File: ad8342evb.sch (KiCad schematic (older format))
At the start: 95 parts, among them J1 PWR_in_direct, J10 Bat, J11 3V3, J12 PWR_Jumper, J13 TP1, J14 TP1, J15 TP_PWR, J16 TP2, J17 TP3, J2 RF_in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

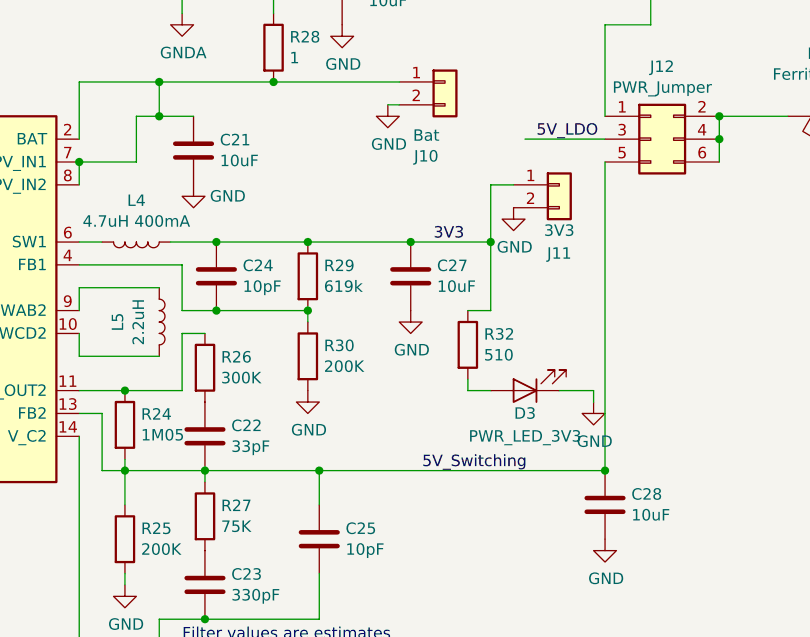
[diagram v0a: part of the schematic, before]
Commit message: fixed mistake in schematic
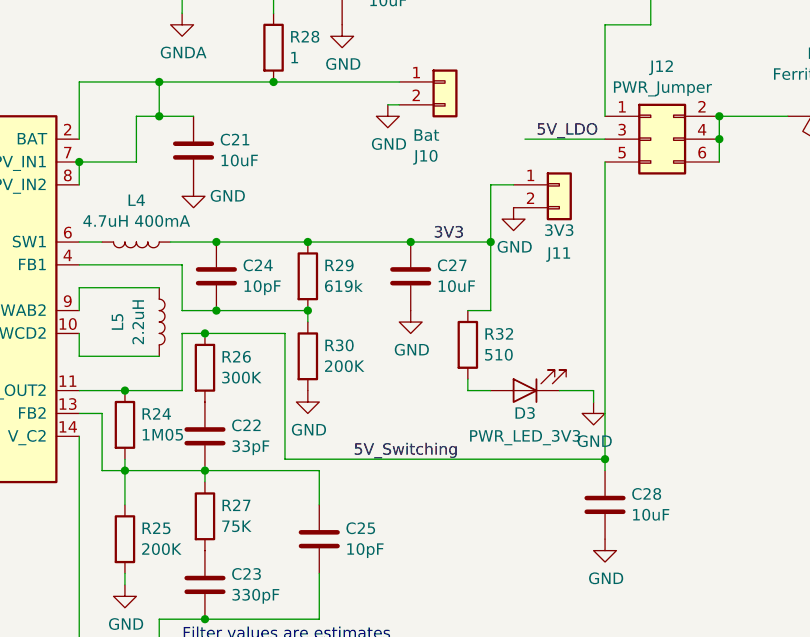
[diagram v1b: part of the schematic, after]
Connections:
- net 5V_Switching: now also R24.1, R26.1, U3.11 (V_OUT2); no longer C22.2, C25.1, R24.2, R25.1, R27.1, U3.13 (FB2)
- new net: C22.2, C25.1, R24.2, R25.1, R27.1, U3.13 (FB2)
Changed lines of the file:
@@
 	4200 7000 4700 7000
 Wire Wire Line
-	5950 5650 5950 7000
-Connection ~ 5950 7000
+	5950 5650 5950 6950
 $Comp
 L Device:C C25
@@
 Wire Wire Line
 	4700 7000 4700 7150
-Connection ~ 4700 7000
-Wire Wire Line
-	4700 7000 5950 7000
 Wire Wire Line
 	4700 7450 4700 7650
@@
 Text Label 5200 6000 0    50   ~ 0
 3V3
-Text Label 5150 7000 0    50   ~ 0
+Text Label 4850 6950 0    50   ~ 0
 5V_Switching
 Connection ~ 5100 6000
@@
 	3650 7750 3650 6850
 Connection ~ 4200 7650
+Wire Wire Line
+	4200 6400 4550 6400
+Wire Wire Line
+	4550 6400 4550 6950
+Wire Wire Line
+	4550 6950 5950 6950
+Connection ~ 4200 6400
+Connection ~ 5950 6950
+Wire Wire Line
+	5950 6950 5950 7000
 $EndSCHEMATC

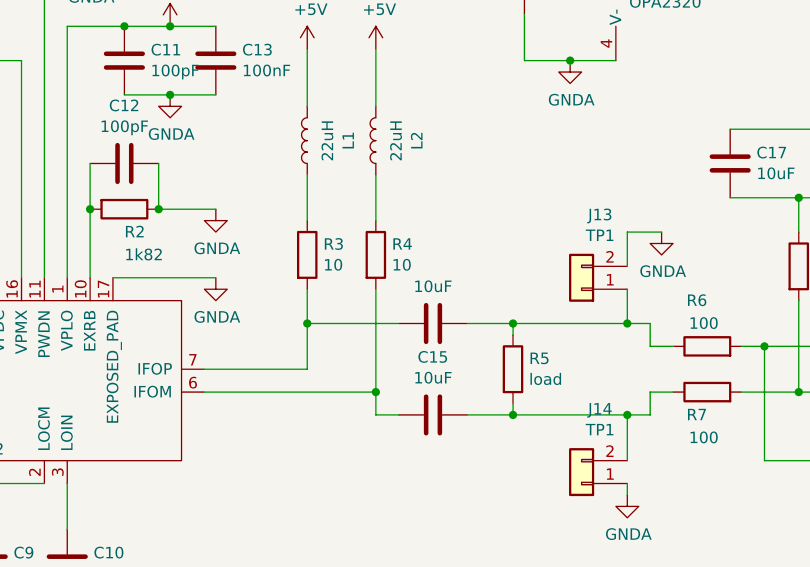
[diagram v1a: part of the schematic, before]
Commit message: added DC bias resistor for OPAMP
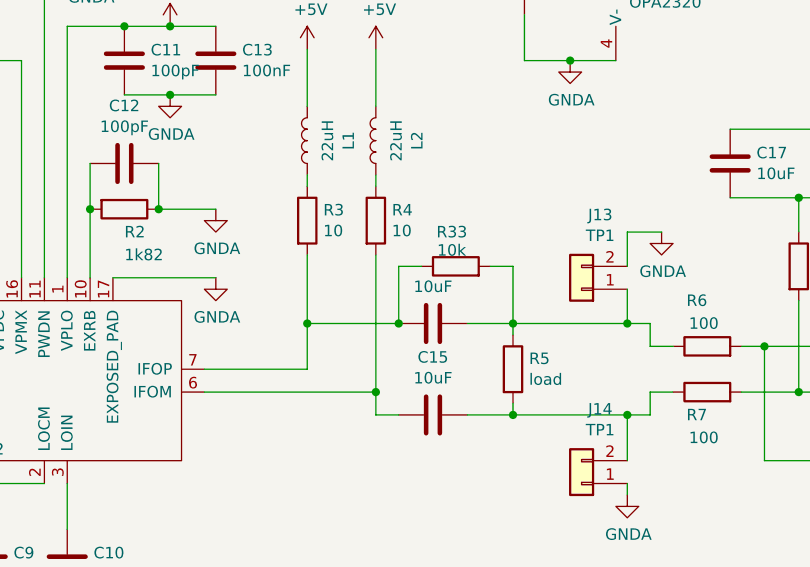
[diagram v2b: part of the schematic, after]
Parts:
- added R33: 10k, Resistor_SMD:R_0805_2012Metric_Pad1.15x1.40mm_HandSolder, symbol Device:R
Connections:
- net at C14.1, R3.2, U4.7 (IFOP): now also R33.1
- net at C14.2, J13.1 (Pin_1), R5.1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: now also R33.2
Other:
- moved on the sheet: R3, R4
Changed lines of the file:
@@
 L Device:R R3
 U 1 1 5F19B732
-P 5450 2500
-F 0 "R3" H 5520 2546 50  0000 L CNN
-F 1 "10" H 5520 2455 50  0000 L CNN
-F 2 "Resistor_SMD:R_0805_2012Metric_Pad1.15x1.40mm_HandSolder" V 5380 2500 50  0001 C CNN
-F 3 "~" H 5450 2500 50  0001 C CNN
-	1    5450 2500
+P 5450 2350
+F 0 "R3" H 5520 2396 50  0000 L CNN
+F 1 "10" H 5520 2305 50  0000 L CNN
+F 2 "Resistor_SMD:R_0805_2012Metric_Pad1.15x1.40mm_HandSolder" V 5380 2350 50  0001 C CNN
+F 3 "~" H 5450 2350 50  0001 C CNN
+	1    5450 2350
 	1    0    0    -1
 $EndComp
@@
 L Device:R R4
 U 1 1 5F19BCA9
-P 5750 2500
-F 0 "R4" H 5820 2546 50  0000 L CNN
-F 1 "10" H 5820 2455 50  0000 L CNN
-F 2 "Resistor_SMD:R_0805_2012Metric_Pad1.15x1.40mm_HandSolder" V 5680 2500 50  0001 C CNN
-F 3 "~" H 5750 2500 50  0001 C CNN
-	1    5750 2500
-	1    0    0    -1
-$EndComp
-Wire Wire Line
-	5450 2650 5450 2800
+P 5750 2350
+F 0 "R4" H 5820 2396 50  0000 L CNN
+F 1 "10" H 5820 2305 50  0000 L CNN
+F 2 "Resistor_SMD:R_0805_2012Metric_Pad1.15x1.40mm_HandSolder" V 5680 2350 50  0001 C CNN
+F 3 "~" H 5750 2350 50  0001 C CNN
+	1    5750 2350
+	1    0    0    -1
+$EndComp
 Wire Wire Line
 	5450 2800 5850 2800
-Wire Wire Line
-	5750 2650 5750 3100
 $Comp
 L power:+5V #PWR0104
@@
 	1    0    0    -1
 $EndComp
-Wire Wire Line
-	5750 2150 5750 2350
 Wire Wire Line
 	4100 2600 4100 1950
@@
 Wire Wire Line
 	750  6200 750  6650
-Wire Wire Line
-	5450 2350 5450 2150
 $Comp
 L Connector_Generic:Conn_02x03_Odd_Even J4
@@
 Wire Wire Line
 	5950 6950 5950 7000
+Wire Wire Line
+	5750 2150 5750 2200
+Wire Wire Line
+	5450 2150 5450 2200
+Wire Wire Line
+	5450 2500 5450 2800
+Wire Wire Line
+	5750 2500 5750 3100
+$Comp
+L Device:R R33
+U 1 1 5F36EBE7
+P 6100 2550
+F 0 "R33" V 6250 2500 50  0000 L CNN
+F 1 "10k" V 6170 2505 50  0000 L CNN
+F 2 "Resistor_SMD:R_0805_2012Metric_Pad1.15x1.40mm_HandSolder" V 6030 2550 50  0001 C CNN
+F 3 "~" H 6100 2550 50  0001 C CNN
+	1    6100 2550
+	0    -1   -1   0
+$EndComp
+Wire Wire Line
+	5950 2550 5850 2550
+Wire Wire Line
+	5850 2550 5850 2800
+Connection ~ 5850 2800
+Wire Wire Line
+	6250 2550 6350 2550
+Wire Wire Line
+	6350 2550 6350 2800
 $EndSCHEMATC

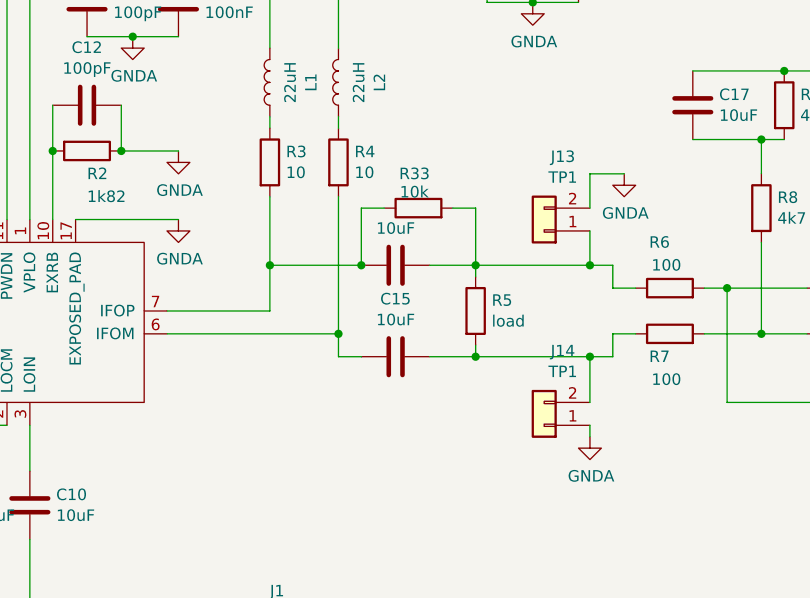
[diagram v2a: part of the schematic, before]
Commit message: moved bias resistor to correct location
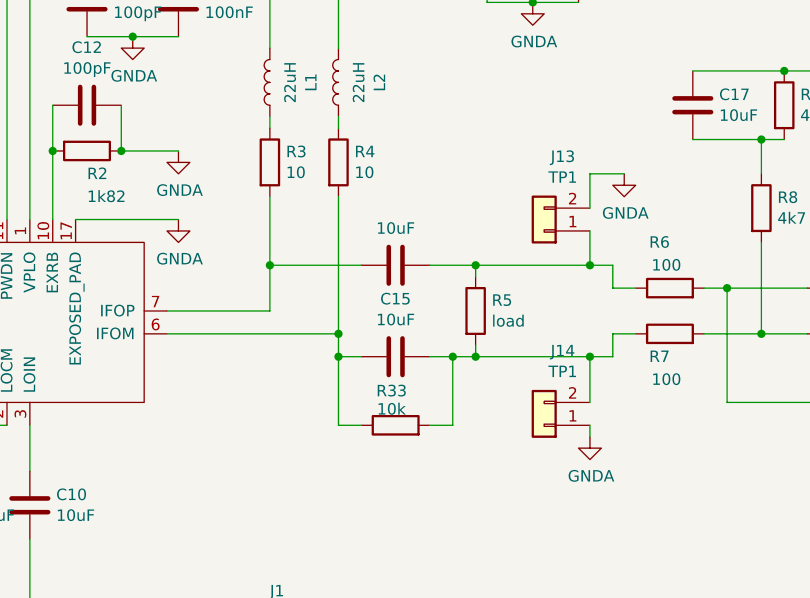
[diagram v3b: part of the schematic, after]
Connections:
- net at C15.1, R4.2, U4.6 (IFOM): now also R33.1
- net at C14.1, R3.2, U4.7 (IFOP): no longer R33.1
- net at C14.2, J13.1 (Pin_1), R5.1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: no longer R33.2
- net at C15.2, J14.2 (Pin_2), R5.2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: now also R33.2
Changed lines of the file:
@@
 	6350 3150 6350 3200
 Wire Wire Line
-	6350 3200 6150 3200
+	6350 3200 6250 3200
 $Comp
 L user_Operational_Amplifier:OPA2320 U2
@@
 $Comp
 L Device:R R33
-U 1 1 5F36EBE7
-P 6100 2550
-F 0 "R33" V 6250 2500 50  0000 L CNN
-F 1 "10k" V 6170 2505 50  0000 L CNN
-F 2 "Resistor_SMD:R_0805_2012Metric_Pad1.15x1.40mm_HandSolder" V 6030 2550 50  0001 C CNN
-F 3 "~" H 6100 2550 50  0001 C CNN
-	1    6100 2550
+U 1 1 5F30BE35
+P 6000 3500
+F 0 "R33" V 6150 3450 50  0000 L CNN
+F 1 "10k" V 6070 3455 50  0000 L CNN
+F 2 "Resistor_SMD:R_0805_2012Metric_Pad1.15x1.40mm_HandSolder" V 5930 3500 50  0001 C CNN
+F 3 "~" H 6000 3500 50  0001 C CNN
+	1    6000 3500
 	0    -1   -1   0
 $EndComp
 Wire Wire Line
-	5950 2550 5850 2550
-Wire Wire Line
-	5850 2550 5850 2800
-Connection ~ 5850 2800
-Wire Wire Line
-	6250 2550 6350 2550
-Wire Wire Line
-	6350 2550 6350 2800
+	5850 3500 5750 3500
+Wire Wire Line
+	6150 3500 6250 3500
+Wire Wire Line
+	5750 3500 5750 3200
+Connection ~ 5750 3200
+Wire Wire Line
+	6250 3500 6250 3200
+Connection ~ 6250 3200
+Wire Wire Line
+	6250 3200 6150 3200
 $EndSCHEMATC

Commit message: modified bias circuit
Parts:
- removed R9: 4k7, Resistor_SMD:R_0805_2012Metric_Pad1.15x1.40mm_HandSolder, symbol Device:R
- added R?: 10k, Resistor_SMD:R_0805_2012Metric_Pad1.15x1.40mm_HandSolder, symbol Device:R
- R33: value 10k -> x
- R8: value 4k7 -> 10k
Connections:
- net +5V: now also R?.2
- net GNDA: now also R8.1
- net at R7.2, R8.2, U2.3 (+): now also C17.2, R?.1
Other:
- moved on the sheet: C17, R10, R8
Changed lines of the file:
@@
 L Device:R R10
 U 1 1 5F1FA385
-P 8000 3400
-F 0 "R10" V 7900 3350 50  0000 L CNN
-F 1 "4k7" V 7800 3350 50  0000 L CNN
-F 2 "Resistor_SMD:R_0805_2012Metric_Pad1.15x1.40mm_HandSolder" V 7930 3400 50  0001 C CNN
-F 3 "~" H 8000 3400 50  0001 C CNN
-	1    8000 3400
+P 8000 2550
+F 0 "R10" V 7900 2500 50  0000 L CNN
+F 1 "4k7" V 7800 2500 50  0000 L CNN
+F 2 "Resistor_SMD:R_0805_2012Metric_Pad1.15x1.40mm_HandSolder" V 7930 2550 50  0001 C CNN
+F 3 "~" H 8000 2550 50  0001 C CNN
+	1    8000 2550
 	0    -1   -1   0
 $EndComp
-Wire Wire Line
-	8400 3000 8400 3400
-Wire Wire Line
-	8400 3400 8150 3400
 $Comp
 L Device:R R8
 U 1 1 5F200A58
-P 7600 2550
-F 0 "R8" H 7670 2596 50  0000 L CNN
-F 1 "4k7" H 7670 2505 50  0000 L CNN
-F 2 "Resistor_SMD:R_0805_2012Metric_Pad1.15x1.40mm_HandSolder" V 7530 2550 50  0001 C CNN
-F 3 "~" H 7600 2550 50  0001 C CNN
-	1    7600 2550
-	1    0    0    -1
+P 7550 3700
+F 0 "R8" H 7650 3650 50  0000 L CNN
+F 1 "10k" H 7650 3750 50  0000 L CNN
+F 2 "Resistor_SMD:R_0805_2012Metric_Pad1.15x1.40mm_HandSolder" V 7480 3700 50  0001 C CNN
+F 3 "~" H 7550 3700 50  0001 C CNN
+	1    7550 3700
+	1    0    0    1
 $EndComp
 $Comp
@@
 	9300 4250 9300 4400
 Wire Wire Line
-	8400 3400 8400 3750
-Wire Wire Line
 	8400 3750 8050 3750
 Wire Wire Line
 	8050 3750 8050 4250
-Connection ~ 8400 3400
 Wire Wire Line
 	9300 4250 9300 3750
@@
 L Device:C C17
 U 1 1 5F280D97
-P 7300 2100
-F 0 "C17" H 7415 2146 50  0000 L CNN
-F 1 "10uF" H 7415 2055 50  0000 L CNN
-F 2 "Capacitor_SMD:C_0805_2012Metric_Pad1.15x1.40mm_HandSolder" H 7338 1950 50  0001 C CNN
-F 3 "~" H 7300 2100 50  0001 C CNN
-	1    7300 2100
-	1    0    0    -1
-$EndComp
-$Comp
-L Device:R R9
-U 1 1 5F284774
-P 7700 2100
-F 0 "R9" H 7770 2146 50  0000 L CNN
-F 1 "4k7" H 7770 2055 50  0000 L CNN
-F 2 "Resistor_SMD:R_0805_2012Metric_Pad1.15x1.40mm_HandSolder" V 7630 2100 50  0001 C CNN
-F 3 "~" H 7700 2100 50  0001 C CNN
-	1    7700 2100
-	1    0    0    -1
-$EndComp
-Wire Wire Line
-	7300 2250 7600 2250
-Wire Wire Line
-	7600 2400 7600 2250
-Connection ~ 7600 2250
-Wire Wire Line
-	7600 2250 7700 2250
-Wire Wire Line
-	7300 1950 7700 1950
+P 7150 3700
+F 0 "C17" H 7250 3650 50  0000 L CNN
+F 1 "10uF" H 7250 3750 50  0000 L CNN
+F 2 "Capacitor_SMD:C_0805_2012Metric_Pad1.15x1.40mm_HandSolder" H 7188 3550 50  0001 C CNN
+F 3 "~" H 7150 3700 50  0001 C CNN
+	1    7150 3700
+	1    0    0    1
+$EndComp
 Wire Wire Line
 	9300 4700 9300 4800
-Wire Wire Line
-	8100 1950 8100 2050
-Wire Wire Line
-	8100 1950 7700 1950
-Connection ~ 7700 1950
 $Comp
 L Device:R R16
@@
 Wire Wire Line
 	8250 4250 8350 4250
-Wire Wire Line
-	7350 2900 7450 2900
-Wire Wire Line
-	7350 3100 7600 3100
-Wire Wire Line
-	7600 2700 7600 3100
-Connection ~ 7600 3100
-Wire Wire Line
-	7600 3100 7800 3100
-Wire Wire Line
-	7450 3400 7450 2900
-Wire Wire Line
-	7450 3400 7850 3400
-Connection ~ 7450 2900
-Wire Wire Line
-	7450 2900 7800 2900
 $Comp
 L Device:R R32
@@
 L power:GNDA #PWR0111
 U 1 1 5F336EFE
-P 8100 2050
-F 0 "#PWR0111" H 8100 1800 50  0001 C CNN
-F 1 "GNDA" H 8105 1877 50  0000 C CNN
-F 2 "" H 8100 2050 50  0001 C CNN
-F 3 "" H 8100 2050 50  0001 C CNN
-	1    8100 2050
-	1    0    0    -1
+P 7350 3850
+F 0 "#PWR0111" H 7350 3600 50  0001 C CNN
+F 1 "GNDA" H 7355 3677 50  0000 C CNN
+F 2 "" H 7350 3850 50  0001 C CNN
+F 3 "" H 7350 3850 50  0001 C CNN
+	1    7350 3850
+	-1   0    0    -1
 $EndComp
 $Comp
@@
 P 6000 3500
 F 0 "R33" V 6150 3450 50  0000 L CNN
-F 1 "10k" V 6070 3455 50  0000 L CNN
+F 1 "x" V 6070 3455 50  0000 L CNN
 F 2 "Resistor_SMD:R_0805_2012Metric_Pad1.15x1.40mm_HandSolder" V 5930 3500 50  0001 C CNN
 F 3 "~" H 6000 3500 50  0001 C CNN
@@
 Wire Wire Line
 	6250 3200 6150 3200
+Connection ~ 7350 3100
+Wire Wire Line
+	7350 3100 7500 3100
+Wire Wire Line
+	8150 2550 8400 2550
+Wire Wire Line
+	8400 2550 8400 3000
+Connection ~ 8400 3000
+Wire Wire Line
+	8400 3000 8400 3750
+$Comp
+L Device:R R?
+U 1 1 5F4F3D38
+P 7500 2400
+F 0 "R?" H 7600 2350 50  0000 L CNN
+F 1 "10k" H 7600 2450 50  0000 L CNN
+F 2 "Resistor_SMD:R_0805_2012Metric_Pad1.15x1.40mm_HandSolder" V 7430 2400 50  0001 C CNN
+F 3 "~" H 7500 2400 50  0001 C CNN
+	1    7500 2400
+	1    0    0    1
+$EndComp
+Wire Wire Line
+	7350 2900 7700 2900
+Wire Wire Line
+	7700 2900 7700 2550
+Wire Wire Line
+	7700 2550 7850 2550
+Connection ~ 7700 2900
+Wire Wire Line
+	7700 2900 7800 2900
+Wire Wire Line
+	7500 2550 7500 3100
+Connection ~ 7500 3100
+Wire Wire Line
+	7500 3100 7800 3100
+$Comp
+L power:+5V #PWR?
+U 1 1 5F5852E9
+P 7500 2100
+F 0 "#PWR?" H 7500 1950 50  0001 C CNN
+F 1 "+5V" H 7515 2273 50  0000 C CNN
+F 2 "" H 7500 2100 50  0001 C CNN
+F 3 "" H 7500 2100 50  0001 C CNN
+	1    7500 2100
+	1    0    0    -1
+$EndComp
+Wire Wire Line
+	7500 2100 7500 2250
+Wire Wire Line
+	7150 3550 7350 3550
+Wire Wire Line
+	7150 3850 7350 3850
+Connection ~ 7350 3850
+Wire Wire Line
+	7350 3850 7550 3850
+Wire Wire Line
+	7350 3100 7350 3550
+Connection ~ 7350 3550
+Wire Wire Line
+	7350 3550 7550 3550
 $EndSCHEMATC
